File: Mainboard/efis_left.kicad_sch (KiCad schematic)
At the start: 21 parts, among them J16 R_FD, J17 R_LS, J18 R_CSTR, J19 R_WPT, J20 R_VORD, J21 R_NDB, J22 R_ARPT, J36 RB_ENC, J38 RB_PULL, J39 RB_hPa/inHg, J44 RB_PUSH, J49 RVOR/ADF_1, J50 RVOR/ADF_2, J51 R_MAP_MODE, J53 R_MAP_RANGE, U1 CD74HC4067M, U2 CD74HC4067M

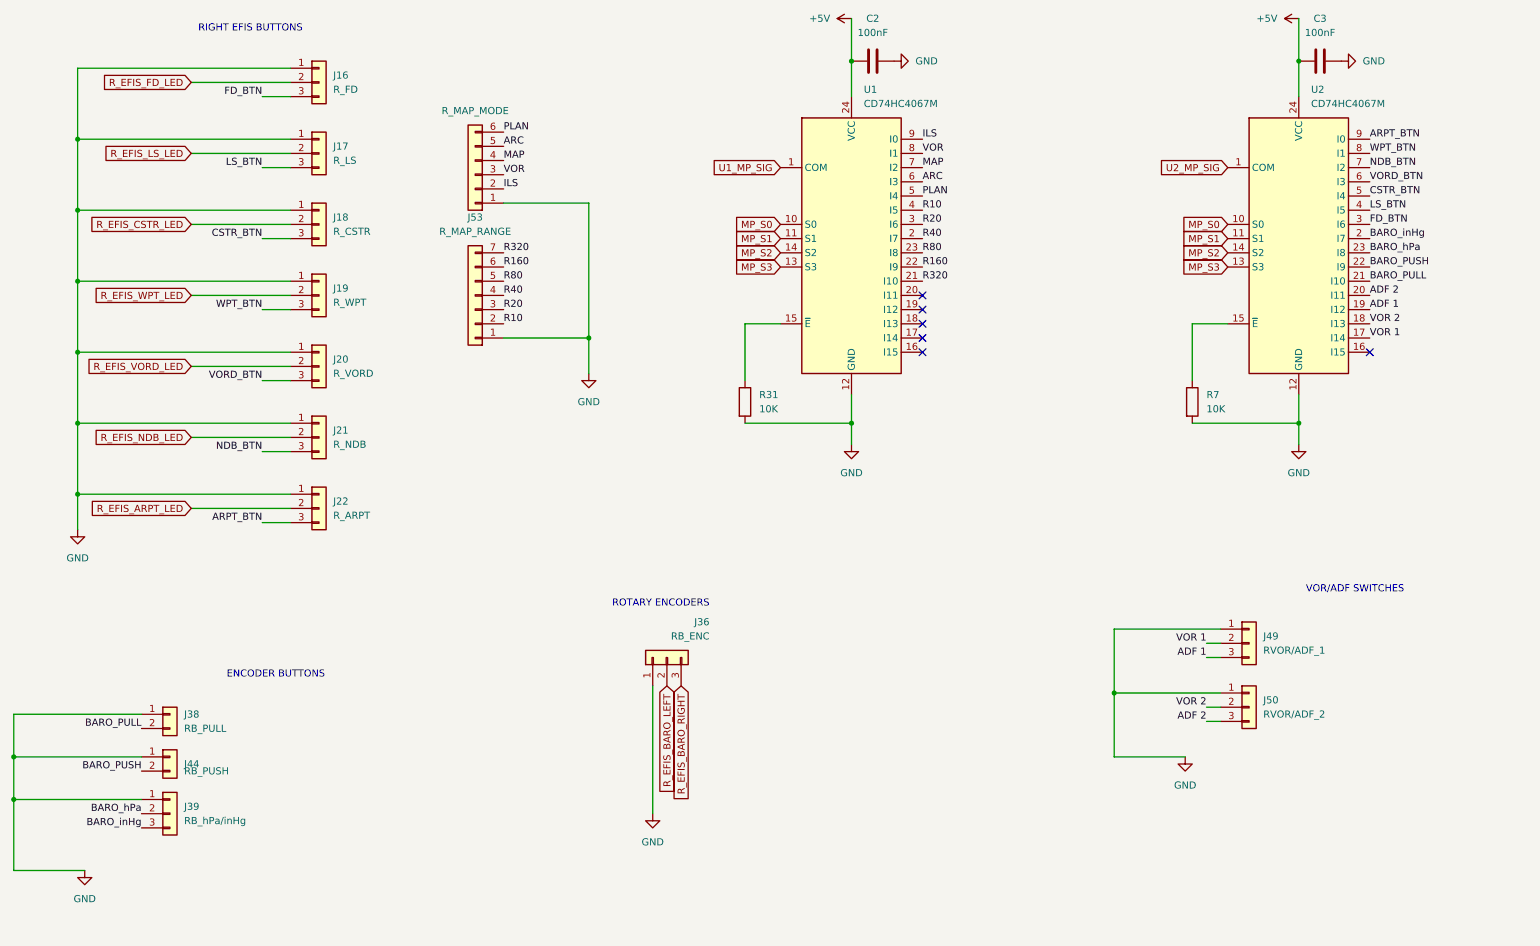
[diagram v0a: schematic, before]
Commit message: Fix the swapped EFIS filenames and rename the backlight nets to +5V
Two naming defects, no electrical change on any board.

EFIS sheets
-----------
The root sheet pointed EFIS_LEFT at efis_right.kicad_sch and EFIS_RIGHT at
efis_left.kicad_sch. The schematic was correct, since the file behind the
LEFT sheet did hold the L_* signals, but the filenames said the opposite and
anyone reading the files from outside KiCad would have been misled.

The two files are swapped and every reference follows: the sheet properties
in the root schematic and the 49 sheetfile entries the footprints carry on
the board. Each file now matches the sheet that loads it.

  netlist   198 nets, 135 components, not one node moved
  ERC       0 violations
  DRC       6 violations, all cosmetic, 0 unconnected, 0 parity issues

Backlight nets
--------------
Every net in the backlighting chain was called +9V while carrying 5 V, on
all four boards. The white LEDs sit behind 91 Ω: at 5 V that is 21 mA, right
at the rating for a 1206 white LED, while 9 V would put them at 65 mA. The
name was a leftover from an earlier design and was the kind of label that
eventually makes someone connect the wrong supply.

Renamed across Korry_Large, Korry_Small, Backlighting_Dimmer and
Backlighting_LEDModule, in both the schematics and the boards: the power
symbol, its value, which is what actually names the net, and the net entries
on the copper. 88 occurrences. None of those boards had a +5V net already,
so nothing was merged.

Verified against the state committed a moment ago: ERC and DRC counts are
identical on all four boards, before and after, and no board gained or lost
a connection.

The Readme drops these two entries and gains the defects that surfaced while
checking: the Backlighting_Dimmer footprints carry their reference in the
value field instead of the schematic value, so a BOM read from that board is
wrong; its terminal block footprint no longer exists in the KiCad library;
four texts on the Korry_Large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
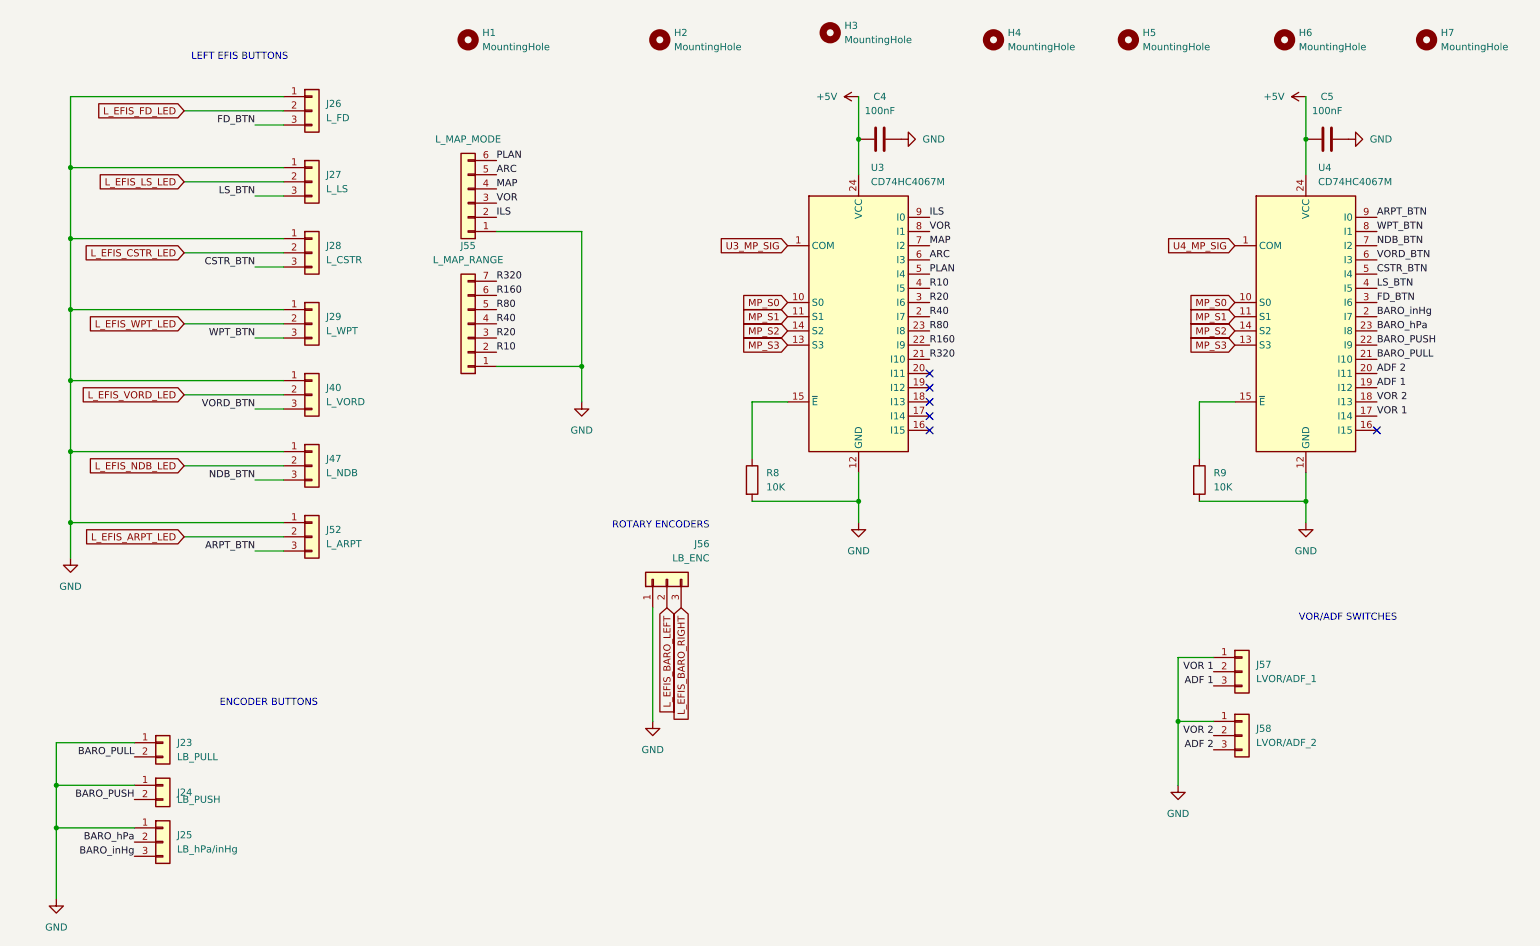
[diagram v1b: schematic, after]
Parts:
- removed C2, C3: 100nF, Capacitor_SMD:C_1206_3216Metric_Pad1.33x1.80mm_HandSolder, symbol Device:C
- removed J16: R_FD, Connector_PinHeader_2.54mm:PinHeader_1x03_P2.54mm_Vertical, symbol Connector_Generic:Conn_01x03
- removed J17: R_LS, Connector_PinHeader_2.54mm:PinHeader_1x03_P2.54mm_Vertical, symbol Connector_Generic:Conn_01x03
- removed J18: R_CSTR, Connector_PinHeader_2.54mm:PinHeader_1x03_P2.54mm_Vertical, symbol Connector_Generic:Conn_01x03
- removed J19: R_WPT, Connector_PinHeader_2.54mm:PinHeader_1x03_P2.54mm_Vertical, symbol Connector_Generic:Conn_01x03
- removed J20: R_VORD, Connector_PinHeader_2.54mm:PinHeader_1x03_P2.54mm_Vertical, symbol Connector_Generic:Conn_01x03
- removed J21: R_NDB, Connector_PinHeader_2.54mm:PinHeader_1x03_P2.54mm_Vertical, symbol Connector_Generic:Conn_01x03
- removed J22: R_ARPT, Connector_PinHeader_2.54mm:PinHeader_1x03_P2.54mm_Vertical, symbol Connector_Generic:Conn_01x03
- removed J36: RB_ENC, Connector_PinHeader_2.54mm:PinHeader_1x03_P2.54mm_Vertical, symbol Connector_Generic:Conn_01x03
- removed J38: RB_PULL, Connector_PinHeader_2.54mm:PinHeader_1x02_P2.54mm_Vertical, symbol Connector_Generic:Conn_01x02
- removed J39: RB_hPa/inHg, Connector_PinHeader_2.54mm:PinHeader_1x03_P2.54mm_Vertical, symbol Connector_Generic:Conn_01x03
- removed J44: RB_PUSH, Connector_PinHeader_2.54mm:PinHeader_1x02_P2.54mm_Vertical, symbol Connector_Generic:Conn_01x02
- removed J49: RVOR/ADF_1, Connector_PinHeader_2.54mm:PinHeader_1x03_P2.54mm_Vertical, symbol Connector_Generic:Conn_01x03
- removed J50: RVOR/ADF_2, Connector_PinHeader_2.54mm:PinHeader_1x03_P2.54mm_Vertical, symbol Connector_Generic:Conn_01x03
- removed J51: R_MAP_MODE, Connector_PinHeader_2.54mm:PinHeader_1x06_P2.54mm_Vertical, symbol Connector_Generic:Conn_01x06
- removed J53: R_MAP_RANGE, Connector_PinHeader_2.54mm:PinHeader_1x07_P2.54mm_Vertical, symbol Connector_Generic:Conn_01x07
- removed R31, R7: 10K, Resistor_SMD:R_1206_3216Metric_Pad1.30x1.75mm_HandSolder, symbol Device:R
- removed U1, U2: CD74HC4067M, Package_SO:SOIC-24W_7.5x15.4mm_P1.27mm, symbol 74xx:CD74HC4067M
- added C4, C5: 100nF, Capacitor_SMD:C_1206_3216Metric_Pad1.33x1.80mm_HandSolder, symbol Device:C
- added H1, H2, H3, H4, H5, H6, H7: MountingHole, MountingHole:MountingHole_2.7mm_M2.5_DIN965_Pad_TopBottom, symbol Mechanical:MountingHole
- added J23: LB_PULL, Connector_PinHeader_2.54mm:PinHeader_1x02_P2.54mm_Vertical, symbol Connector_Generic:Conn_01x02
- added J24: LB_PUSH, Connector_PinHeader_2.54mm:PinHeader_1x02_P2.54mm_Vertical, symbol Connector_Generic:Conn_01x02
- added J25: LB_hPa/inHg, Connector_PinHeader_2.54mm:PinHeader_1x03_P2.54mm_Vertical, symbol Connector_Generic:Conn_01x03
- added J26: L_FD, Connector_PinHeader_2.54mm:PinHeader_1x03_P2.54mm_Vertical, symbol Connector_Generic:Conn_01x03
- added J27: L_LS, Connector_PinHeader_2.54mm:PinHeader_1x03_P2.54mm_Vertical, symbol Connector_Generic:Conn_01x03
- added J28: L_CSTR, Connector_PinHeader_2.54mm:PinHeader_1x03_P2.54mm_Vertical, symbol Connector_Generic:Conn_01x03
- added J29: L_WPT, Connector_PinHeader_2.54mm:PinHeader_1x03_P2.54mm_Vertical, symbol Connector_Generic:Conn_01x03
- added J40: L_VORD, Connector_PinHeader_2.54mm:PinHeader_1x03_P2.54mm_Vertical, symbol Connector_Generic:Conn_01x03
- added J47: L_NDB, Connector_PinHeader_2.54mm:PinHeader_1x03_P2.54mm_Vertical, symbol Connector_Generic:Conn_01x03
- added J52: L_ARPT, Connector_PinHeader_2.54mm:PinHeader_1x03_P2.54mm_Vertical, symbol Connector_Generic:Conn_01x03
- added J54: L_MAP_MODE, Connector_PinHeader_2.54mm:PinHeader_1x06_P2.54mm_Vertical, symbol Connector_Generic:Conn_01x06
- added J55: L_MAP_RANGE, Connector_PinHeader_2.54mm:PinHeader_1x07_P2.54mm_Vertical, symbol Connector_Generic:Conn_01x07
- added J56: LB_ENC, Connector_PinHeader_2.54mm:PinHeader_1x03_P2.54mm_Vertical, symbol Connector_Generic:Conn_01x03
- added J57: LVOR/ADF_1, Connector_PinHeader_2.54mm:PinHeader_1x03_P2.54mm_Vertical, symbol Connector_Generic:Conn_01x03
- added J58: LVOR/ADF_2, Connector_PinHeader_2.54mm:PinHeader_1x03_P2.54mm_Vertical, symbol Connector_Generic:Conn_01x03
- added R8, R9: 10K, Resistor_SMD:R_1206_3216Metric_Pad1.30x1.75mm_HandSolder, symbol Device:R
- added U3, U4: CD74HC4067M, Package_SO:SOIC-24W_7.5x15.4mm_P1.27mm, symbol 74xx:CD74HC4067M
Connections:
- net +5V: now also C4.1, C5.1, U3.24 (VCC), U4.24 (VCC)
- net ADF 1: now also J57.3 (Pin_3), U4.19 (I12)
- net ADF 2: now also J58.3 (Pin_3), U4.20 (I11)
- net ARC: now also J54.5 (Pin_5), U3.6 (I3)
- net ARPT_BTN: now also J52.3 (Pin_3), U4.9 (I0)
- net BARO_PULL: now also J23.2 (Pin_2), U4.21 (I10)
- net BARO_PUSH: now also J24.2 (Pin_2), U4.22 (I9)
- net BARO_hPa: now also J25.2 (Pin_2), U4.23 (I8)
- net BARO_inHg: now also J25.3 (Pin_3), U4.2 (I7)
- net CSTR_BTN: now also J28.3 (Pin_3), U4.5 (I4)
- net FD_BTN: now also J26.3 (Pin_3), U4.3 (I6)
- net GND: now also C4.2, C5.2, J23.1 (Pin_1), J24.1 (Pin_1), J25.1 (Pin_1), J26.1 (Pin_1), J27.1 (Pin_1), J28.1 (Pin_1), J29.1 (Pin_1), J40.1 (Pin_1), J47.1 (Pin_1), J52.1 (Pin_1), J54.1 (Pin_1), J55.1 (Pin_1), J56.1 (Pin_1), J57.1 (Pin_1), J58.1 (Pin_1), R8.2, R9.2, U3.12 (GND), U4.12 (GND)
- net ILS: now also J54.2 (Pin_2), U3.9 (I0)
- net LS_BTN: now also J27.3 (Pin_3), U4.4 (I5)
- net MAP: now also J54.4 (Pin_4), U3.7 (I2)
- net MP_S0: now also U3.10 (S0), U4.10 (S0)
- net MP_S1: now also U3.11 (S1), U4.11 (S1)
- net MP_S2: now also U3.14 (S2), U4.14 (S2)
- net MP_S3: now also U3.13 (S3), U4.13 (S3)
- net NDB_BTN: now also J47.3 (Pin_3), U4.7 (I2)
- net PLAN: now also J54.6 (Pin_6), U3.5 (I4)
- net R10: now also J55.2 (Pin_2), U3.4 (I5)
- net R160: now also J55.6 (Pin_6), U3.22 (I9)
- net R20: now also J55.3 (Pin_3), U3.3 (I6)
- net R320: now also J55.7 (Pin_7), U3.21 (I10)
- net R40: now also J55.4 (Pin_4), U3.2 (I7)
- net R80: now also J55.5 (Pin_5), U3.23 (I8)
- net VOR: now also J54.3 (Pin_3), U3.8 (I1)
- net VOR 1: now also J57.2 (Pin_2), U4.17 (I14)
- net VOR 2: now also J58.2 (Pin_2), U4.18 (I13)
- net VORD_BTN: now also J40.3 (Pin_3), U4.6 (I3)
- net WPT_BTN: now also J29.3 (Pin_3), U4.8 (I1)
- new net: R8.1, U3.15 (~{E})
- new net: R9.1, U4.15 (~{E})
- new net L_EFIS_ARPT_LED: J52.2 (Pin_2)
- new net L_EFIS_BARO_LEFT: J56.2 (Pin_2)
- new net L_EFIS_BARO_RIGHT: J56.3 (Pin_3)
- new net L_EFIS_CSTR_LED: J28.2 (Pin_2)
- new net L_EFIS_FD_LED: J26.2 (Pin_2)
- new net L_EFIS_LS_LED: J27.2 (Pin_2)
- new net L_EFIS_NDB_LED: J47.2 (Pin_2)
- new net L_EFIS_VORD_LED: J40.2 (Pin_2)
- new net L_EFIS_WPT_LED: J29.2 (Pin_2)
- new net U3_MP_SIG: U3.1 (COM)
- new net U4_MP_SIG: U4.1 (COM)
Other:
- note added: "LEFT EFIS BUTTONS"
- note removed: "RIGHT EFIS BUTTONS"
